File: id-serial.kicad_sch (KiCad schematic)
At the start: 5 parts

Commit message: Rename files and change title block
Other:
- company: Antmicro Ltd -> Capable Robot Components, Inc.
- title: Jetson Nano Baseboard -> Capable Jetson Carrier
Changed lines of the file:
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@@
   (paper "A3")
   (title_block
-    (title "Jetson Nano Baseboard")
-    (date "2022-02-04")
-    (rev "1.5.1")
-    (company "Antmicro Ltd")
-    (comment 1 "www.antmicro.com")
-    (comment 2 "Antmicro Ltd")
+    (title "Capable Jetson Carrier")
+    (date "2022-04-06")
+    (rev "v1.0")
+    (company "Capable Robot Components, Inc.")
+    (comment 1 "www.capablerobot.com")
+    (comment 2 "")
   )
   (junction (at 218.44 120.015) (diameter 0) (color 0 0 0 0)

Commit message: Rebuild
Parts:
- removed R132: (no value), symbol jetson-nano-baseboard:R_0R_0402
- removed TP30: (no value), symbol jetson-nano-baseboard:TC2030
- C36: value (none) -> C_100n_0402; footprint (none) -> jetson-nano-baseboard-footprints:0402-cap
- D15: value (none) -> diode; footprint (none) -> jetson-nano-baseboard-footprints:SOD-323
- IC17: value (none) -> AT24CS01-ST; footprint (none) -> jetson-nano-baseboard-footprints:SOT23-5
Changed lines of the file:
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@@
     (company "Capable Robot Components, Inc.")
     (comment 1 "www.capablerobot.com")
-    (comment 2 "")
   )
   (junction (at 218.44 120.015) (diameter 0) (color 0 0 0 0)
@@
     (stroke (width 0) (type default) (color 0 0 0 0))
   )
-  (wire (pts (xy 172.72 165.1) (xy 194.31 165.1))
-    (stroke (width 0) (type default) (color 0 0 0 0))
-  )
-  (wire (pts (xy 194.31 172.72) (xy 178.435 172.72))
-    (stroke (width 0) (type default) (color 0 0 0 0))
-  )
-  (wire (pts (xy 194.31 162.56) (xy 193.04 162.56))
-    (stroke (width 0) (type default) (color 0 0 0 0))
-  )
-  (wire (pts (xy 194.31 167.64) (xy 172.72 167.64))
-    (stroke (width 0) (type default) (color 0 0 0 0))
-  )
-  (wire (pts (xy 178.435 172.72) (xy 178.435 173.355))
-    (stroke (width 0) (type default) (color 0 0 0 0))
-  )
   (wire (pts (xy 177.165 122.555) (xy 191.135 122.555))
     (stroke (width 0) (type default) (color 0 0 0 0))
@@
   )
   (wire (pts (xy 247.65 140.97) (xy 247.65 143.51))
-    (stroke (width 0) (type default) (color 0 0 0 0))
-  )
-  (wire (pts (xy 172.72 170.18) (xy 194.31 170.18))
-    (stroke (width 0) (type default) (color 0 0 0 0))
-  )
-  (wire (pts (xy 172.72 162.56) (xy 185.42 162.56))
     (stroke (width 0) (type default) (color 0 0 0 0))
   )
@@
   )
   (wire (pts (xy 216.535 120.015) (xy 218.44 120.015))
-    (stroke (width 0) (type default) (color 0 0 0 0))
-  )
-  (wire (pts (xy 172.72 160.02) (xy 194.31 160.02))
     (stroke (width 0) (type default) (color 0 0 0 0))
   )
@@
     (effects (font (size 1.524 1.524)) (justify left bottom))
   )
-  (label "SN_WP" (at 172.72 162.56 0)
-    (effects (font (size 1.524 1.524)) (justify left bottom))
-  )
   (label "EEPROM_PWR" (at 234.315 120.015 180)
     (effects (font (size 1.524 1.524)) (justify right bottom))
@@
     (effects (font (size 1.524 1.524)) (justify left bottom))
   )
-  (label "EEPROM_PWR" (at 172.72 160.02 0)
-    (effects (font (size 1.524 1.524)) (justify left bottom))
-  )
   (label "SN_WP" (at 177.165 125.095 0)
-    (effects (font (size 1.524 1.524)) (justify left bottom))
-  )
-  (label "GEN0_SDA" (at 172.72 170.18 0)
-    (effects (font (size 1.524 1.524)) (justify left bottom))
-  )
-  (label "GEN0_SDA" (at 172.72 165.1 0)
-    (effects (font (size 1.524 1.524)) (justify left bottom))
-  )
-  (label "GEN0_SCL" (at 172.72 167.64 0)
     (effects (font (size 1.524 1.524)) (justify left bottom))
   )
@@
       (effects (font (size 1.524 1.524)) (justify left bottom))
     )
-    (property "Value" "" (id 1) (at 196.215 130.175 0)
+    (property "Value" "AT24CS01-ST" (id 1) (at 196.215 130.175 0)
       (effects (font (size 1.524 1.524)) (justify left bottom))
     )
-    (property "Footprint" "" (id 2) (at 196.215 130.175 0)
+    (property "Footprint" "jetson-nano-baseboard-footprints:SOT23-5" (id 2) (at 196.215 130.175 0)
       (effects (font (size 1.524 1.524)) hide)
     )
@@
       (effects (font (size 0.508 0.508)) hide)
     )
-    (property "Value" "" (id 1) (at 216.4842 131.3942 0)
+    (property "Value" "GND" (id 1) (at 216.4842 131.3942 0)
       (effects (font (size 0.762 0.762)))
     )
@@
       (effects (font (size 0.508 0.508)) hide)
     )
-    (property "Value" "" (id 1) (at 247.65 146.9136 0)
+    (property "Value" "GND" (id 1) (at 247.65 146.9136 0)
       (effects (font (size 0.762 0.762)))
     )
@@
       (effects (font (size 1.524 1.524)) (justify right))
     )
-    (property "Value" "" (id 1) (at 220.472 114.3762 0)
+    (property "Value" "diode" (id 1) (at 220.472 114.3762 0)
       (effects (font (size 1.524 1.524)) (justify right) hide)
     )
-    (property "Footprint" "" (id 2) (at 218.44 113.03 0)
+    (property "Footprint" "jetson-nano-baseboard-footprints:SOD-323" (id 2) (at 218.44 113.03 0)
       (effects (font (size 1.524 1.524)) hide)
     )
@@
     (pin "C")
   )
-  (symbol (lib_id "jetson-nano-baseboard:TC2030") (at 207.01 162.56 0) (unit 1)
-    (in_bom yes) (on_board yes)
-    (property "Reference" "TP30" (id 0) (at 200.2536 155.6004 0)
-      (effects (font (size 1.524 1.524)) (justify left))
-    )
-    (property "Value" "" (id 1) (at 201.3204 177.3682 0)
-      (effects (font (size 1.524 1.524)) (justify left))
-    )
-    (property "Footprint" "" (id 2) (at 208.28 147.32 0)
-      (effects (font (size 1.524 1.524)) hide)
-    )
-    (property "Datasheet" "" (id 3) (at 203.2 143.51 0)
-      (effects (font (size 1.524 1.524)) hide)
-    )
-    (property "Manufacturer" "Tag Connect" (id 4) (at 208.28 147.32 0)
-      (effects (font (size 1.27 1.27)) hide)
-    )
-    (property "MPN" "TC2030" (id 5) (at 208.28 147.32 0)
-      (effects (font (size 1.27 1.27)) hide)
-    )
-    (pin "1")
-    (pin "2")
-    (pin "3")
-    (pin "4")
-    (pin "6")
-    (pin "5")
-  )
-  (symbol (lib_id "jetson-nano-baseboard:GND") (at 178.435 173.355 0) (unit 1)
-    (in_bom yes) (on_board yes)
-    (property "Reference" "#GND_0119" (id 0) (at 178.435 173.355 0)
-      (effects (font (size 0.508 0.508)) hide)
-    )
-    (property "Value" "" (id 1) (at 178.3842 176.4792 0)
-      (effects (font (size 0.762 0.762)))
-    )
-    (property "Footprint" "" (id 2) (at 178.435 173.355 0)
-      (effects (font (size 1.778 1.778)) hide)
-    )
-    (property "Datasheet" "" (id 3) (at 178.435 173.355 0)
-      (effects (font (size 1.778 1.778)) hide)
-    )
-    (pin "1")
-  )
-  (symbol (lib_id "jetson-nano-baseboard:R_0R_0402") (at 189.23 162.56 0) (unit 1)
-    (in_bom yes) (on_board yes)
-    (property "Reference" "R132" (id 0) (at 183.515 161.29 0)
-      (effects (font (size 1.524 1.524)))
-    )
-    (property "Value" "" (id 1) (at 189.23 166.37 0)
-      (effects (font (size 1.524 1.524)) hide)
-    )
-    (property "Footprint" "" (id 2) (at 194.31 157.48 0)
-      (effects (font (size 1.524 1.524)) (justify left) hide)
-    )
-    (property "Datasheet" "" (id 3) (at 189.23 162.56 0)
-      (effects (font (size 1.27 1.27)) hide)
-    )
-    (property "Manufacturer" "PANASONIC" (id 4) (at 194.31 152.4 0)
-      (effects (font (size 1.524 1.524)) (justify left) hide)
-    )
-    (property "MPN" "ERJ2GE0R00X" (id 5) (at 194.31 154.94 0)
-      (effects (font (size 1.524 1.524)) (justify left) hide)
-    )
-    (property "Val" "0R" (id 6) (at 193.675 161.29 0))
-    (pin "1")
-    (pin "2")
-  )
   (symbol (lib_id "jetson-nano-baseboard:C_100n_0402") (at 247.65 137.16 180) (unit 1)
     (in_bom yes) (on_board yes)
@@
       (effects (font (size 1.524 1.524)) (justify left))
     )
-    (property "Value" "" (id 1) (at 247.65 133.35 0)
+    (property "Value" "C_100n_0402" (id 1) (at 247.65 133.35 0)
       (effects (font (size 1.524 1.524)) hide)
     )
-    (property "Footprint" "" (id 2) (at 242.57 142.24 0)
+    (property "Footprint" "jetson-nano-baseboard-footprints:0402-cap" (id 2) (at 242.57 142.24 0)
       (effects (font (size 1.524 1.524)) (justify left) hide)
     )

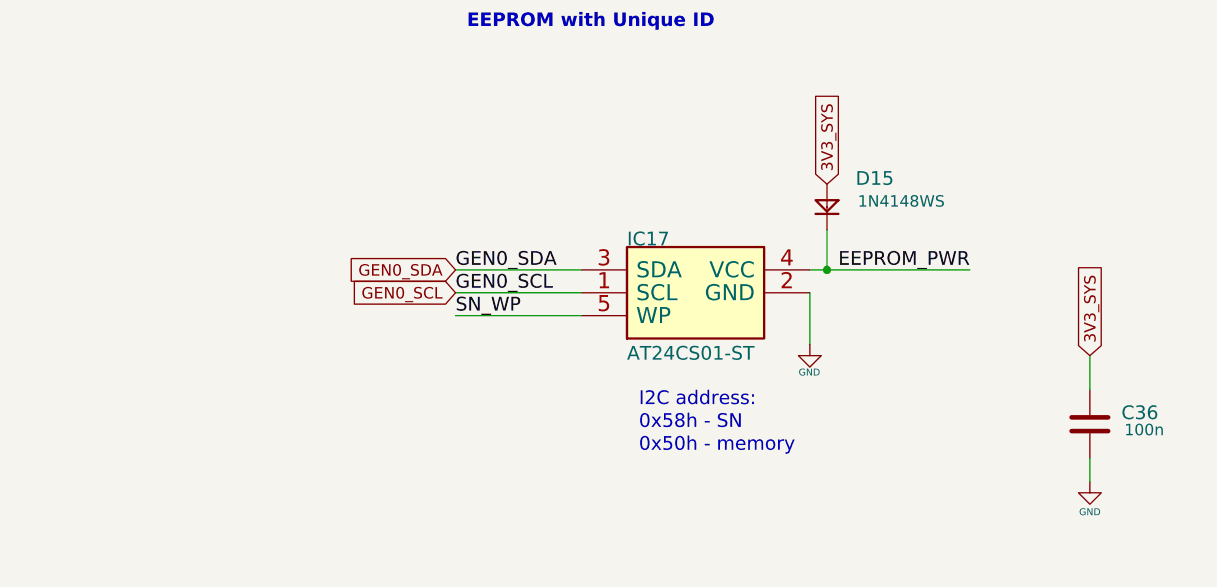
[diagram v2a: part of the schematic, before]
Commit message: Checkpoint.  New camera connectors.  Change to 2242 NVMe drive (not routed yet).
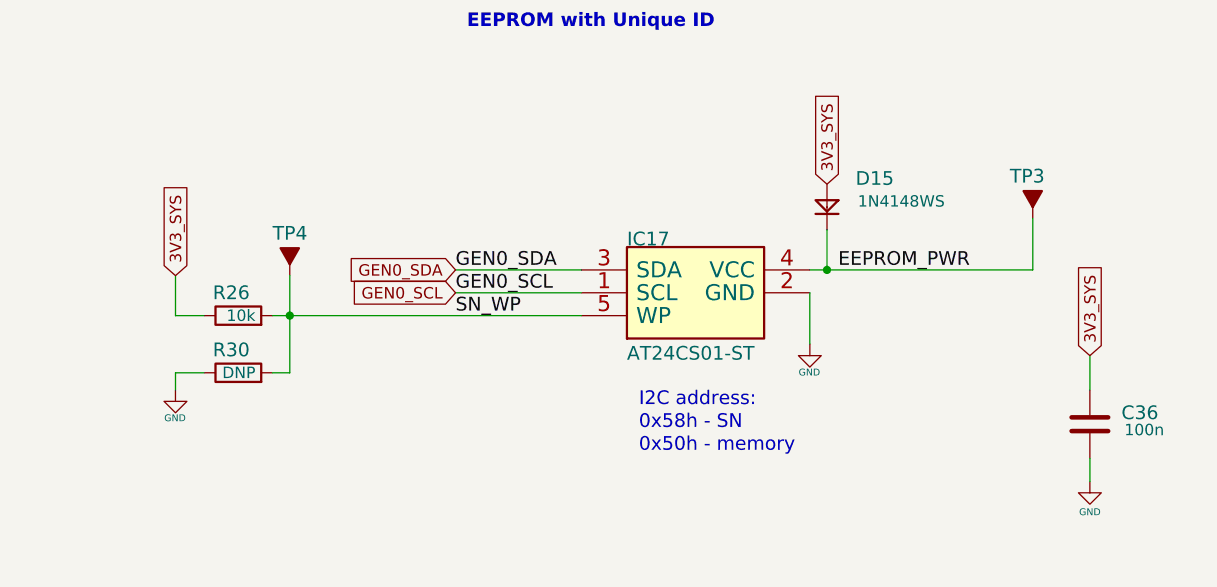
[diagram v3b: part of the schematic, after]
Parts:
- added R26: R_10k_0402, jetson-nano-baseboard-footprints:0402-res, symbol jetson-nano-baseboard:R_2k_0402
- added R30: DNP, jetson-nano-baseboard-footprints:0402-res, symbol jetson-nano-baseboard:R_2k_0402
- added TP3, TP4: Testpad, jetson-nano-baseboard-footprints:TP-R-1.5, symbol jetson-nano-baseboard:Testpad
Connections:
- net 3V3_SYS: now also R26.1
- net EEPROM_PWR: now also TP3.1 (P)
- net GND: now also R30.1
- net SN_WP: now also R26.2, R30.2, TP4.1 (P)
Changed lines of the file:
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@@
     (comment 1 "www.capablerobot.com")
   )
+  (junction (at 158.75 125.095) (diameter 0) (color 0 0 0 0)
+  )
   (junction (at 218.44 120.015) (diameter 0) (color 0 0 0 0)
   )
@@
     (stroke (width 0) (type default) (color 0 0 0 0))
   )
+  (wire (pts (xy 241.3 114.3) (xy 241.3 120.015))
+    (stroke (width 0) (type default) (color 0 0 0 0))
+  )
   (wire (pts (xy 216.535 122.555) (xy 216.535 128.27))
     (stroke (width 0) (type default) (color 0 0 0 0))
   )
+  (wire (pts (xy 218.44 120.015) (xy 241.3 120.015))
+    (stroke (width 0) (type default) (color 0 0 0 0))
+  )
+  (wire (pts (xy 146.05 125.095) (xy 146.05 120.65))
+    (stroke (width 0) (type default) (color 0 0 0 0))
+  )
+  (wire (pts (xy 156.845 131.445) (xy 158.75 131.445))
+    (stroke (width 0) (type default) (color 0 0 0 0))
+  )
+  (wire (pts (xy 156.845 125.095) (xy 158.75 125.095))
+    (stroke (width 0) (type default) (color 0 0 0 0))
+  )
   (wire (pts (xy 177.165 122.555) (xy 191.135 122.555))
     (stroke (width 0) (type default) (color 0 0 0 0))
@@
     (stroke (width 0) (type default) (color 0 0 0 0))
   )
-  (wire (pts (xy 177.165 125.095) (xy 191.135 125.095))
+  (wire (pts (xy 158.75 125.095) (xy 191.135 125.095))
+    (stroke (width 0) (type default) (color 0 0 0 0))
+  )
+  (wire (pts (xy 149.225 131.445) (xy 146.05 131.445))
     (stroke (width 0) (type default) (color 0 0 0 0))
   )
@@
     (stroke (width 0) (type default) (color 0 0 0 0))
   )
-  (wire (pts (xy 218.44 120.015) (xy 234.315 120.015))
+  (wire (pts (xy 158.75 131.445) (xy 158.75 125.095))
     (stroke (width 0) (type default) (color 0 0 0 0))
   )
   (wire (pts (xy 216.535 120.015) (xy 218.44 120.015))
+    (stroke (width 0) (type default) (color 0 0 0 0))
+  )
+  (wire (pts (xy 158.75 120.65) (xy 158.75 125.095))
+    (stroke (width 0) (type default) (color 0 0 0 0))
+  )
+  (wire (pts (xy 149.225 125.095) (xy 146.05 125.095))
+    (stroke (width 0) (type default) (color 0 0 0 0))
+  )
+  (wire (pts (xy 146.05 131.445) (xy 146.05 133.35))
     (stroke (width 0) (type default) (color 0 0 0 0))
   )
@@
   (label "GEN0_SDA" (at 177.165 120.015 0)
     (effects (font (size 1.524 1.524)) (justify left bottom))
+  )
+  (global_label "3V3_SYS" (shape input) (at 146.05 120.65 90) (fields_autoplaced)
+    (effects (font (size 1.27 1.27)) (justify left))
+    (property "Intersheet References" "${INTERSHEET_REFS}" (id 0) (at -72.39 10.16 0)
+      (effects (font (size 1.27 1.27)) hide)
+    )
   )
   (global_label "3V3_SYS" (shape input) (at 247.65 129.54 90) (fields_autoplaced)
@@
     (pin "2")
   )
+  (symbol (lib_id "jetson-nano-baseboard:R_2k_0402") (at 153.035 131.445 0) (unit 1)
+    (in_bom yes) (on_board yes)
+    (property "Reference" "R30" (id 0) (at 154.305 128.905 0)
+      (effects (font (size 1.524 1.524)) (justify right))
+    )
+    (property "Value" "DNP" (id 1) (at 153.035 135.255 0)
+      (effects (font (size 1.524 1.524)) hide)
+    )
+    (property "Footprint" "jetson-nano-baseboard-footprints:0402-res" (id 2) (at 158.115 126.365 0)
+      (effects (font (size 1.524 1.524)) (justify left) hide)
+    )
+    (property "Datasheet" "" (id 3) (at 153.035 131.445 0)
+      (effects (font (size 1.27 1.27)) hide)
+    )
+    (property "Manufacturer" "" (id 4) (at 158.115 121.285 0)
+      (effects (font (size 1.524 1.524)) (justify left) hide)
+    )
+    (property "MPN" "" (id 5) (at 158.115 123.825 0)
+      (effects (font (size 1.524 1.524)) (justify left) hide)
+    )
+    (property "Val" "DNP" (id 6) (at 154.94 131.445 0)
+      (effects (font (size 1.27 1.27)) (justify right))
+    )
+    (pin "1")
+    (pin "2")
+  )
+  (symbol (lib_id "jetson-nano-baseboard:GND") (at 146.05 133.35 0) (unit 1)
+    (in_bom yes) (on_board yes)
+    (property "Reference" "#GND_07" (id 0) (at 146.05 133.35 0)
+      (effects (font (size 0.508 0.508)) hide)
+    )
+    (property "Value" "GND" (id 1) (at 145.9992 136.4742 0)
+      (effects (font (size 0.762 0.762)))
+    )
+    (property "Footprint" "" (id 2) (at 146.05 133.35 0)
+      (effects (font (size 1.778 1.778)) hide)
+    )
+    (property "Datasheet" "" (id 3) (at 146.05 133.35 0)
+      (effects (font (size 1.778 1.778)) hide)
+    )
+    (pin "1")
+  )
+  (symbol (lib_id "jetson-nano-baseboard:Testpad") (at 241.3 113.03 0) (unit 1)
+    (in_bom yes) (on_board yes)
+    (property "Reference" "TP3" (id 0) (at 238.76 109.601 0)
+      (effects (font (size 1.524 1.524)) (justify left))
+    )
+    (property "Value" "Testpad" (id 1) (at 241.3 113.03 0)
+      (effects (font (size 1.524 1.524)) hide)
+    )
+    (property "Footprint" "jetson-nano-baseboard-footprints:TP-R-1.5" (id 2) (at 241.3 113.03 0)
+      (effects (font (size 1.524 1.524)) hide)
+    )
+    (property "Datasheet" "" (id 3) (at 241.3 113.03 0)
+      (effects (font (size 1.524 1.524)) hide)
+    )
+    (property "Manufacturer" "N/A" (id 4) (at 241.3 113.03 0)
+      (effects (font (size 1.27 1.27)) hide)
+    )
+    (property "MPN" "N/A" (id 5) (at 241.3 113.03 0)
+      (effects (font (size 1.27 1.27)) hide)
+    )
+    (pin "1")
+  )
+  (symbol (lib_id "jetson-nano-baseboard:R_2k_0402") (at 153.035 125.095 0) (unit 1)
+    (in_bom yes) (on_board yes)
+    (property "Reference" "R26" (id 0) (at 154.305 122.555 0)
+      (effects (font (size 1.524 1.524)) (justify right))
+    )
+    (property "Value" "R_10k_0402" (id 1) (at 153.035 128.905 0)
+      (effects (font (size 1.524 1.524)) hide)
+    )
+    (property "Footprint" "jetson-nano-baseboard-footprints:0402-res" (id 2) (at 158.115 120.015 0)
+      (effects (font (size 1.524 1.524)) (justify left) hide)
+    )
+    (property "Datasheet" "" (id 3) (at 153.035 125.095 0)
+      (effects (font (size 1.27 1.27)) hide)
+    )
+    (property "Manufacturer" "" (id 4) (at 158.115 114.935 0)
+      (effects (font (size 1.524 1.524)) (justify left) hide)
+    )
+    (property "MPN" "" (id 5) (at 158.115 117.475 0)
+      (effects (font (size 1.524 1.524)) (justify left) hide)
+    )
+    (property "Val" "10k" (id 6) (at 154.94 125.095 0)
+      (effects (font (size 1.27 1.27)) (justify right))
+    )
+    (pin "1")
+    (pin "2")
+  )
+  (symbol (lib_id "jetson-nano-baseboard:Testpad") (at 158.75 119.38 0) (unit 1)
+    (in_bom yes) (on_board yes)
+    (property "Reference" "TP4" (id 0) (at 156.845 115.951 0)
+      (effects (font (size 1.524 1.524)) (justify left))
+    )
+    (property "Value" "Testpad" (id 1) (at 158.75 119.38 0)
+      (effects (font (size 1.524 1.524)) hide)
+    )
+    (property "Footprint" "jetson-nano-baseboard-footprints:TP-R-1.5" (id 2) (at 158.75 119.38 0)
+      (effects (font (size 1.524 1.524)) hide)
+    )
+    (property "Datasheet" "" (id 3) (at 158.75 119.38 0)
+      (effects (font (size 1.524 1.524)) hide)
+    )
+    (property "Manufacturer" "N/A" (id 4) (at 158.75 119.38 0)
+      (effects (font (size 1.27 1.27)) hide)
+    )
+    (property "MPN" "N/A" (id 5) (at 158.75 119.38 0)
+      (effects (font (size 1.27 1.27)) hide)
+    )
+    (pin "1")
+  )
 )
